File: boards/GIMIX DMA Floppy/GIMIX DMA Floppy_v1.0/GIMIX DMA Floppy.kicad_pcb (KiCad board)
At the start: 2 copper layers, 248.9 x 139.7 mm, 138 parts, among them J1 Floppy 5.25", J2 Floppy 8", P1 SS-50 Bus, Q1 LM7805_TO220, Q2 LM7805_TO220, SW1 SW_DIP_x10, SW2 SW_DIP_x10, U1 74LS244, U10 74LS393, U11 7404, U12 74LS74, U14 74LS08, U19 WD2797, U2 7438, U20 4538, U22 74LS123, U23 7406, U24 74LS74, U25 74LS74, U26 74LS367, U27 74LS138, U28 74LS273, U29 74LS174, U3 7438, U30 74LS161, U31 74LS161, U32 74LS161, U33 74LS161, U34 74LS240, U35 74LS240, U36 74F04, U37 7420, U38 74LS367, U39 74LS32, U4 7406, U40 74LS136, U41 74LS136, U42 74LS136, U43 74LS136, U44 74LS136, U45 74LS244, U46 74LS244, U47 74LS533, U48 74LS244, U5 7406, U52 74LS132, U54 74LS161, U55 7406, U59 74LS74, U6 74LS08, U7 74LS08, U8 74LS157, U9 74LS221, Y1 ?

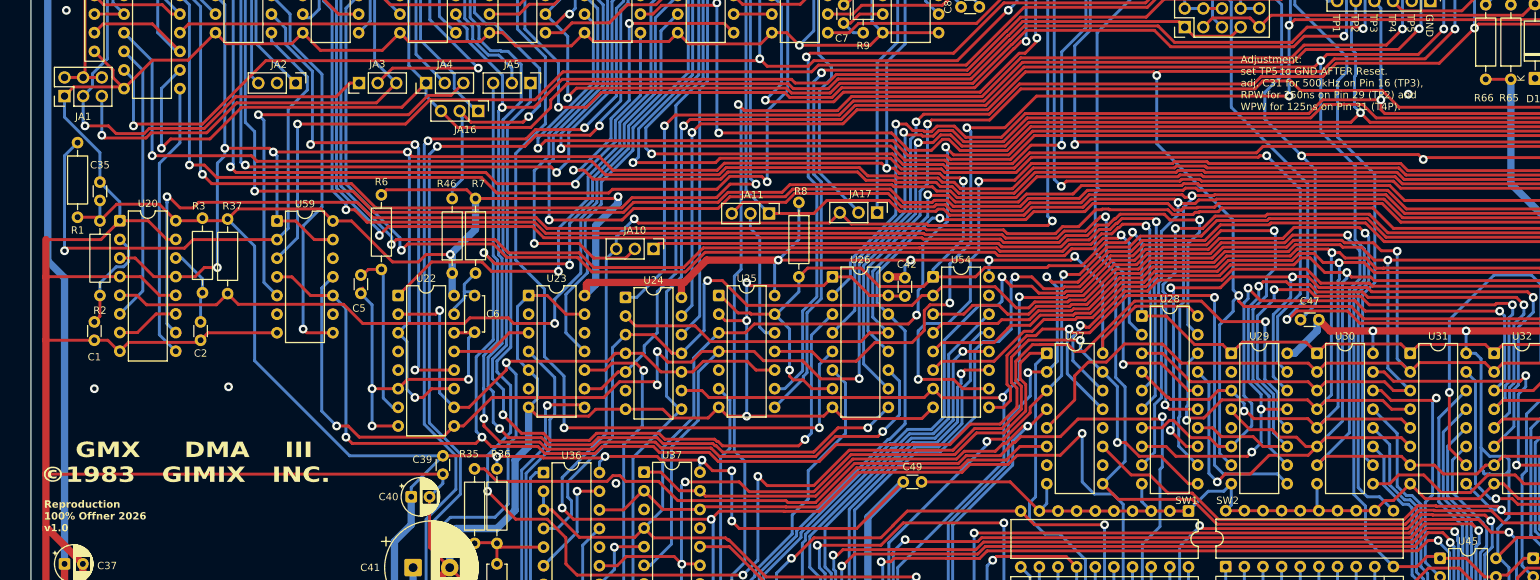
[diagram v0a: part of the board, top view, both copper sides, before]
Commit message: DMA Floppy silkscreen update
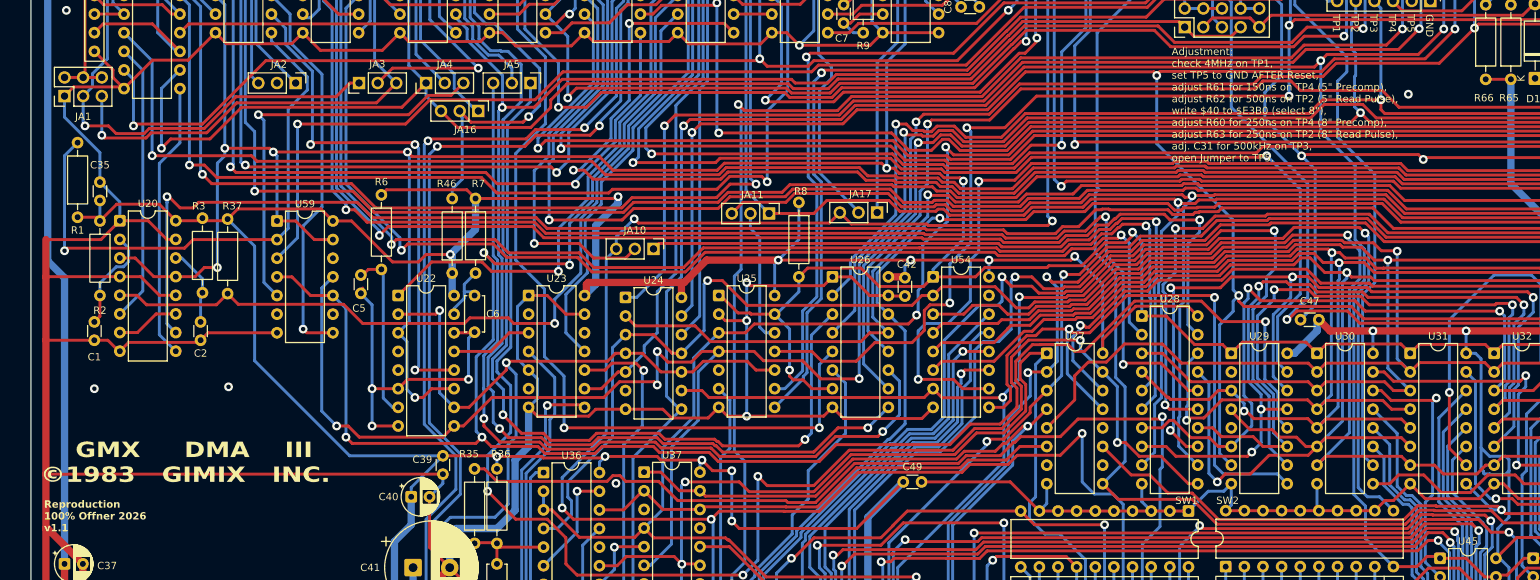
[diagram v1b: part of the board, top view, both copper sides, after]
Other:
- board text added: "Adjustment: check 4MHz on TP1, set TP5 to GND AFTER Reset, adjust R61 for 150ns on TP4 (5{dblquote} Precomp), adjust R62 for 500ns on TP2 (5{dblquote} Read Pulse), write $40 to $E3B0 (select 8{dblquote}), adjust R60 for 250ns on TP4 (8{dblquote} Precomp), adjust R63 for 250ns on TP2 (8{dblquote} Read Pulse), adj. C31 for 500kHz on TP3, open Jumper to TP5."
- board text added: "Reproduction 100% Offner 2026 v1.1"
- board text removed: "Adjustment: set TP5 to GND AFTER Reset. adj. C31 for 500kHz on Pin 16 (TP3), RPW for 250ns on Pin 29 (TP2) and WPW for 125ns on Pin 31 (T4P)."
- board text removed: "Reproduction 100% Offner 2026 v1.0"
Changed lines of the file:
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@@
 		)
 	)
-	(gr_text "Adjustment:\nset TP5 to GND AFTER Reset.\nadj. C31 for 500kHz on Pin 16 (TP3),\nRPW for 250ns on Pin 29 (TP2) and\nWPW for 125ns on Pin 31 (T4P)."
-		(at 183.896 71.12 0)
+	(gr_text "Adjustment:\ncheck 4MHz on TP1,\nset TP5 to GND AFTER Reset,\nadjust R61 for 150ns on TP4 (5{dblquote} Precomp),\nadjust R62 for 500ns on TP2 (5{dblquote} Read Pulse),\nwrite $40 to $E3B0 (select 8{dblquote}),\nadjust R60 for 250ns on TP4 (8{dblquote} Precomp),\nadjust R63 for 250ns on TP2 (8{dblquote} Read Pulse),\nadj. C31 for 500kHz on TP3,\nopen Jumper to TP5."
+		(at 174.498 78.105 0)
 		(layer "F.SilkS")
 		(effects
@@
 		)
 	)
-	(gr_text "Reproduction \n100% Offner 2026\nv1.0"
+	(gr_text "Reproduction \n100% Offner 2026\nv1.1"
 		(at 20.828 128.524 0)
 		(layer "F.SilkS")
